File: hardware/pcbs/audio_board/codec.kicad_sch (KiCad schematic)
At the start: 9 parts, among them U2 SGTL5000XNLA3

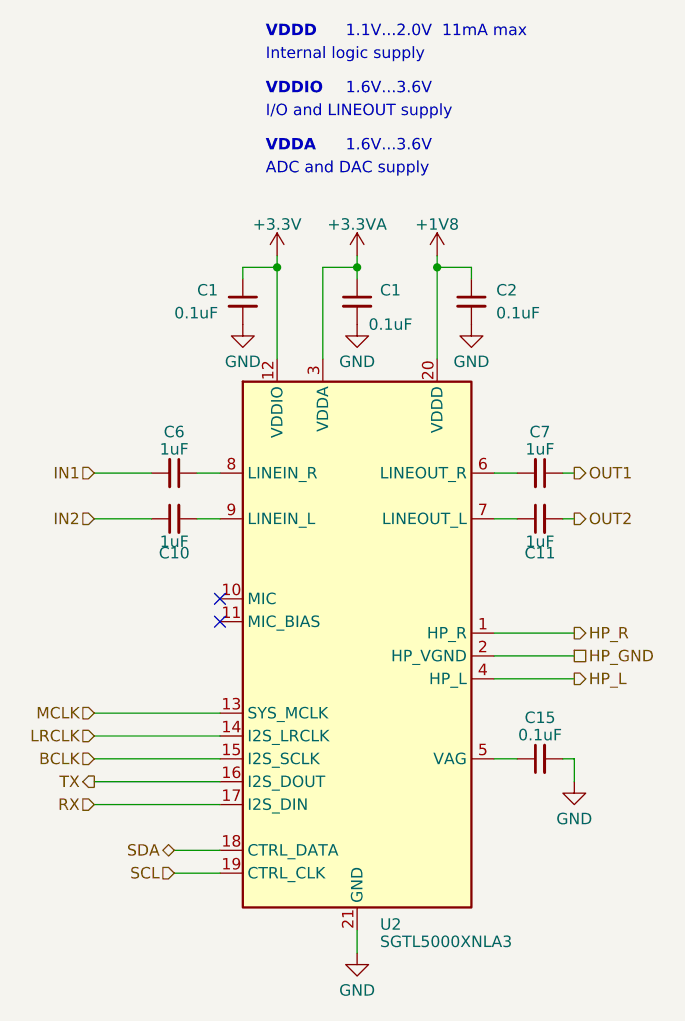
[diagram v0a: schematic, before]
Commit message: Small audio board fixes and add DHAN-M module
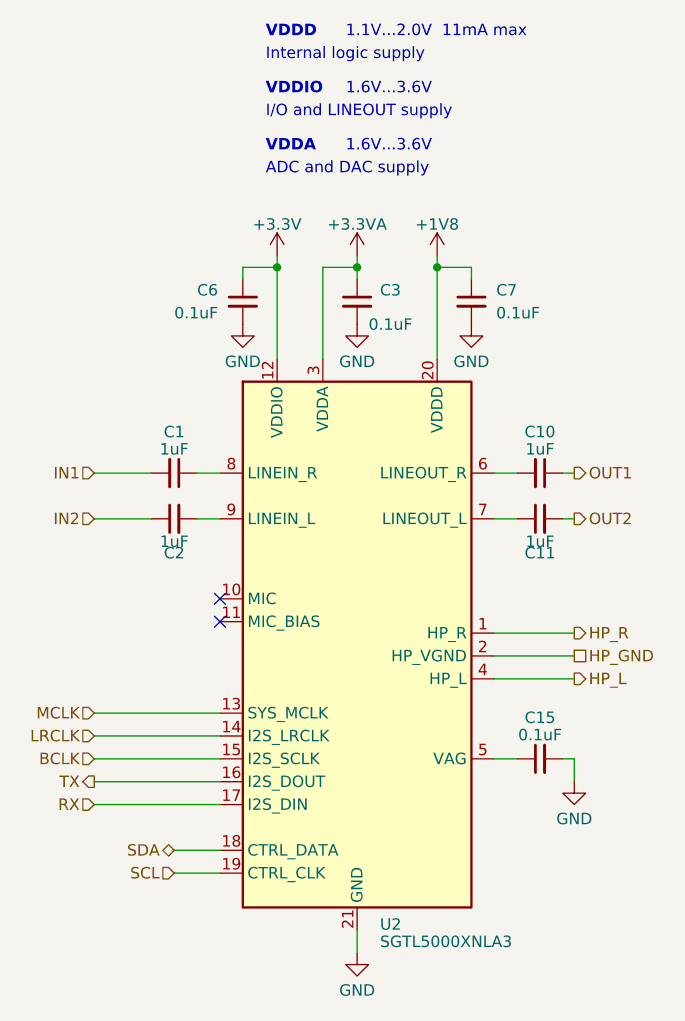
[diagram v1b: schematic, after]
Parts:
- renumbered C6 to C1, C7 to C10, C10 to C2, C1 to C3, C1 to C6, C2 to C7

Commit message: audio_board, power_board: update shop and part links
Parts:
- C1, C10, C11, C2: Part (none) -> C 1μF 16V 0603
- C15, C3, C6, C7: Part (none) -> C 100nF 16V 0603
- U2: Part (none) -> SGTL5000XNLA3R2; Shop (none) -> https://eu.mouser.com/ProductDetail/NXP-Semiconductors/SGTL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
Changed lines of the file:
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@@
+			)
+		)
+		(property "Part" "C 1μF 16V 0603"
+			(at 162.56 82.55 0)
+			(effects
+				(font
+					(size 1.27 1.27)
+				)
+				(hide yes)
 			)
 		)
@@
 			)
 		)
+		(property "Part" "C 1μF 16V 0603"
+			(at 162.56 87.63 0)
+			(effects
+				(font
+					(size 1.27 1.27)
+				)
+				(hide yes)
+			)
+		)
 		(pin "1"
 		)
@@
 			)
 		)
+		(property "Part" "C 100nF 16V 0603"
+			(at 154.94 63.5 0)
+			(effects
+				(font
+					(size 1.27 1.27)
+				)
+				(hide yes)
+			)
+		)
 		(pin "1"
 		)
@@
 			)
 		)
+		(property "Part" "C 100nF 16V 0603"
+			(at 142.24 63.5 0)
+			(effects
+				(font
+					(size 1.27 1.27)
+				)
+				(hide yes)
+			)
+		)
 		(pin "1"
 		)
@@
 			)
 		)
+		(property "Part" "C 1μF 16V 0603"
+			(at 121.92 82.55 0)
+			(effects
+				(font
+					(size 1.27 1.27)
+				)
+				(hide yes)
+			)
+		)
 		(pin "1"
 		)
@@
 		)
 		(property "LCSC" "C14663"
+			(at 129.54 63.5 0)
+			(effects
+				(font
+					(size 1.27 1.27)
+				)
+				(hide yes)
+			)
+		)
+		(property "Part" "C 100nF 16V 0603"
 			(at 129.54 63.5 0)
 			(effects
@@
 			)
 		)
+		(property "Part" "SGTL5000XNLA3R2 "
+			(at 142.24 97.79 0)
+			(effects
+				(font
+					(size 1.27 1.27)
+				)
+				(hide yes)
+			)
+		)
+		(property "Shop" "https://eu.mouser.com/ProductDetail/NXP-Semiconductors/SGTL5000XNLA3R2?qs=g5o6z0NmdpRyTqz1GkwAeA%3D%3D"
+			(at 142.24 97.79 0)
+			(effects
+				(font
+					(size 1.27 1.27)
+				)
+				(hide yes)
+			)
+		)
 		(pin "1"
 		)
@@
 			)
 		)
+		(property "Part" "C 100nF 16V 0603"
+			(at 162.56 114.3 0)
+			(effects
+				(font
+					(size 1.27 1.27)
+				)
+				(hide yes)
+			)
+		)
 		(pin "1"
 		)
@@
 			(at 121.92 87.63 0)
 			(effects
+				(font
+					(size 1.27 1.27)
+				)
+				(hide yes)
+			)
+		)
+		(property "Part" "C 1μF 16V 0603"
+			(at 121.92 87.63 0)
+			(effects

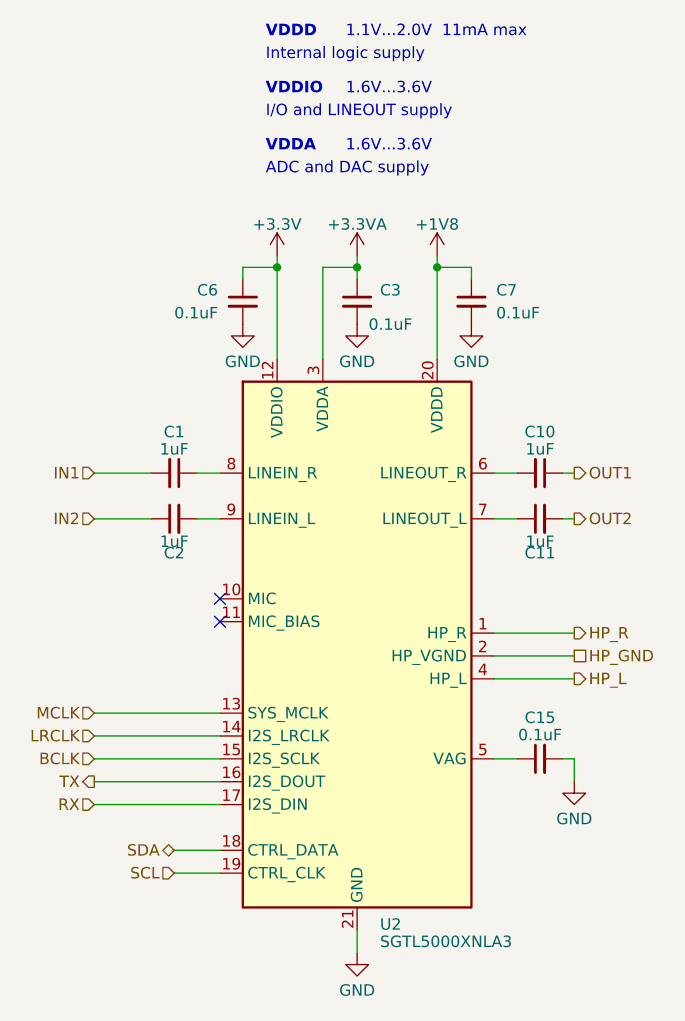
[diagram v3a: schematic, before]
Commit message: pcbs: update purchase info
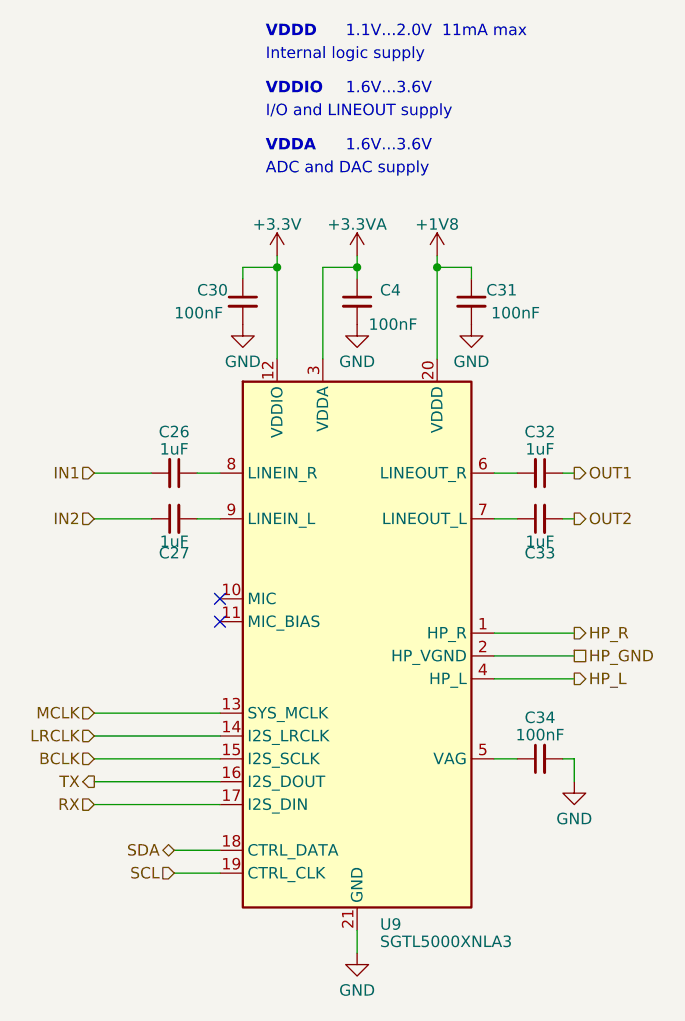
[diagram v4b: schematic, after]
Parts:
- C26: renamed from C1; Shop (none) -> https://store.comet.bg/Catalogue/Product/18391/
- C27: renamed from C2; Shop (none) -> https://store.comet.bg/Catalogue/Product/18391/
- C30: renamed from C6; value 0.1uF -> 100nF; Shop (none) -> https://store.comet.bg/Catalogue/Product/38000/
- C31: renamed from C7; value 0.1uF -> 100nF; Shop (none) -> https://store.comet.bg/Catalogue/Product/38000/
- C32: renamed from C10; Shop (none) -> https://store.comet.bg/Catalogue/Product/18391/
- C33: renamed from C11; Shop (none) -> https://store.comet.bg/Catalogue/Product/18391/
- C34: renamed from C15; value 0.1uF -> 100nF; Shop (none) -> https://store.comet.bg/Catalogue/Product/38000/
- C4: renamed from C3; value 0.1uF -> 100nF; Shop (none) -> https://store.comet.bg/Catalogue/Product/38000/
- renumbered U2 to U9
